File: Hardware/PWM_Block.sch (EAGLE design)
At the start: 51 parts, among them U1 PCA9685, U2 PCA9306, U3 EDISON_CONNECTOR_FULLMOUNTING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, U4 EDISON_CONNECTOR_FULLHEADER

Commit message: Added DCIN pin Corrected Header footprint Renamed board and files Cleaned up dimensions and added units Added VSYS -> VIN circuit Added DNP to pullup resistors
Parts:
- added D1: B340A, SparkFun-DiscreteSemi:DIODE-SCHOTTKY-B340A
- added SJ7: VIN_ENABLE, SparkFun-Passives:JUMPER-PAD-2-NOYES_SILK
- R4, R5: value 2.2k -> DNP
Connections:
- new net DCIN: U3.DCIN, U4.DCIN
- new net N$2: D1.C, SJ7.1
- net VCC: now also SJ7.2
- net VSYS: now also D1.A
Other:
- note added: "v02"
- note removed: "01"
- moved on the sheet: C1, C2, C3, R1, R2, R3, R4, R5, U2

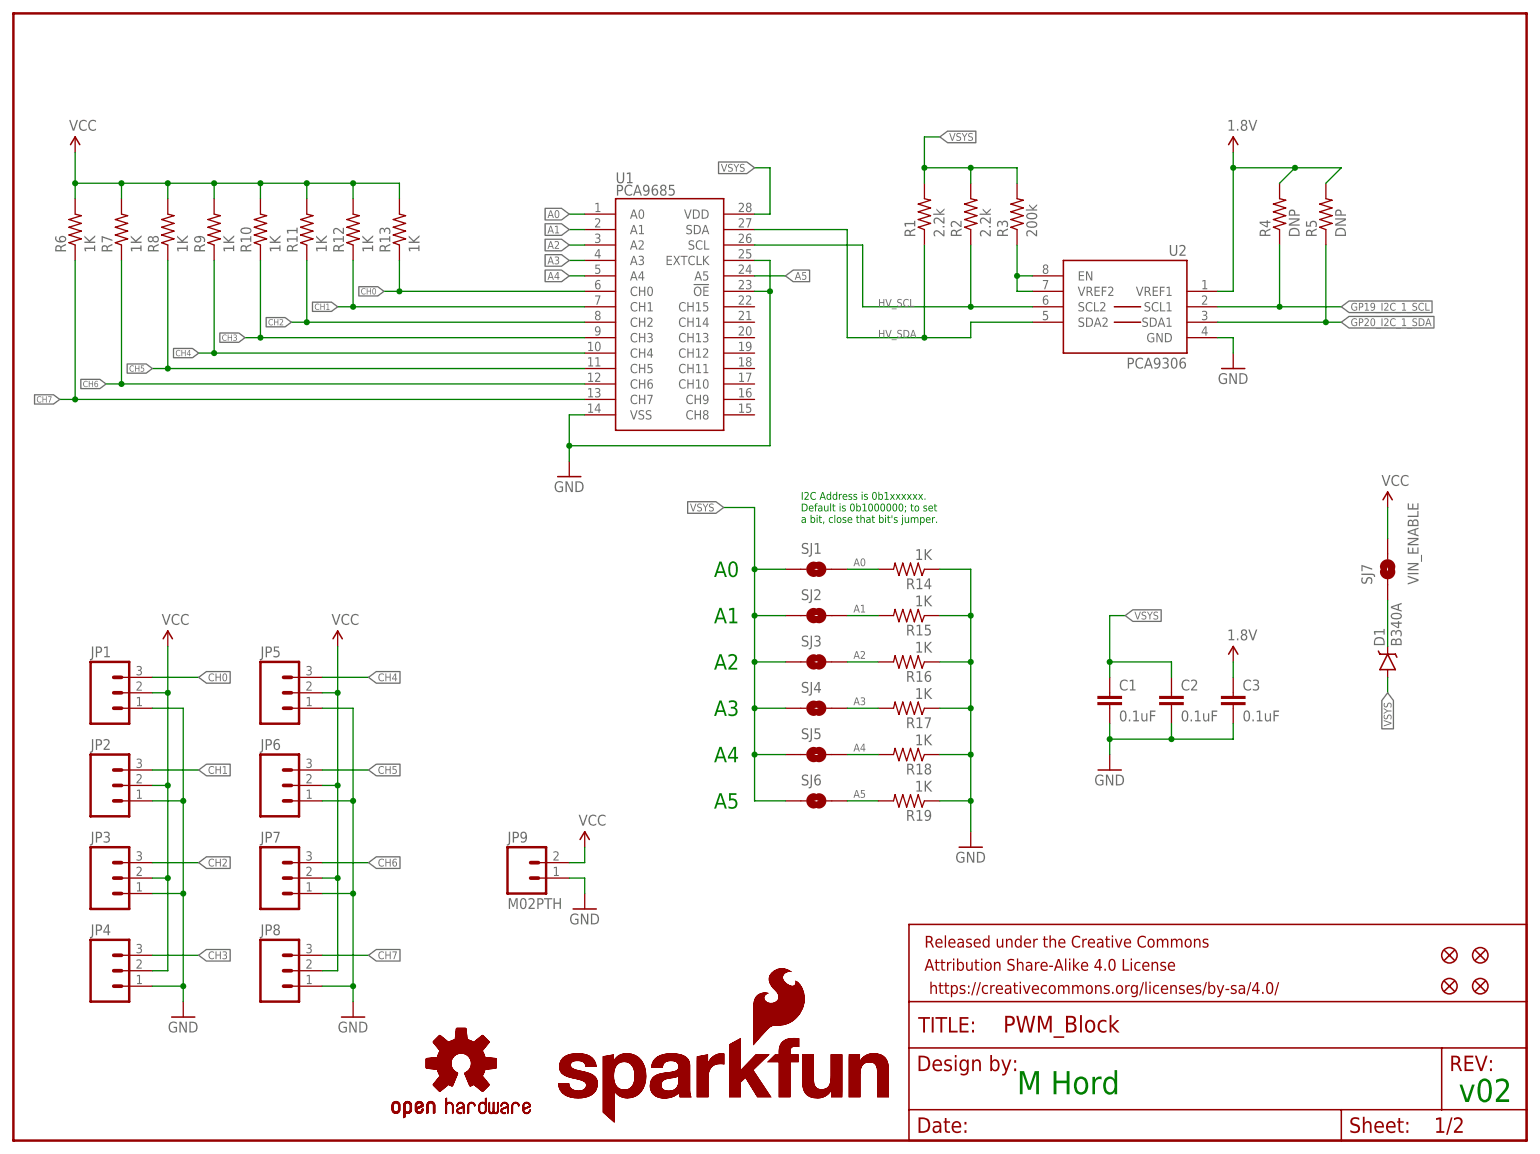
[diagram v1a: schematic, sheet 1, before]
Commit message: Rev to 10. Fix gnd and pwr, text
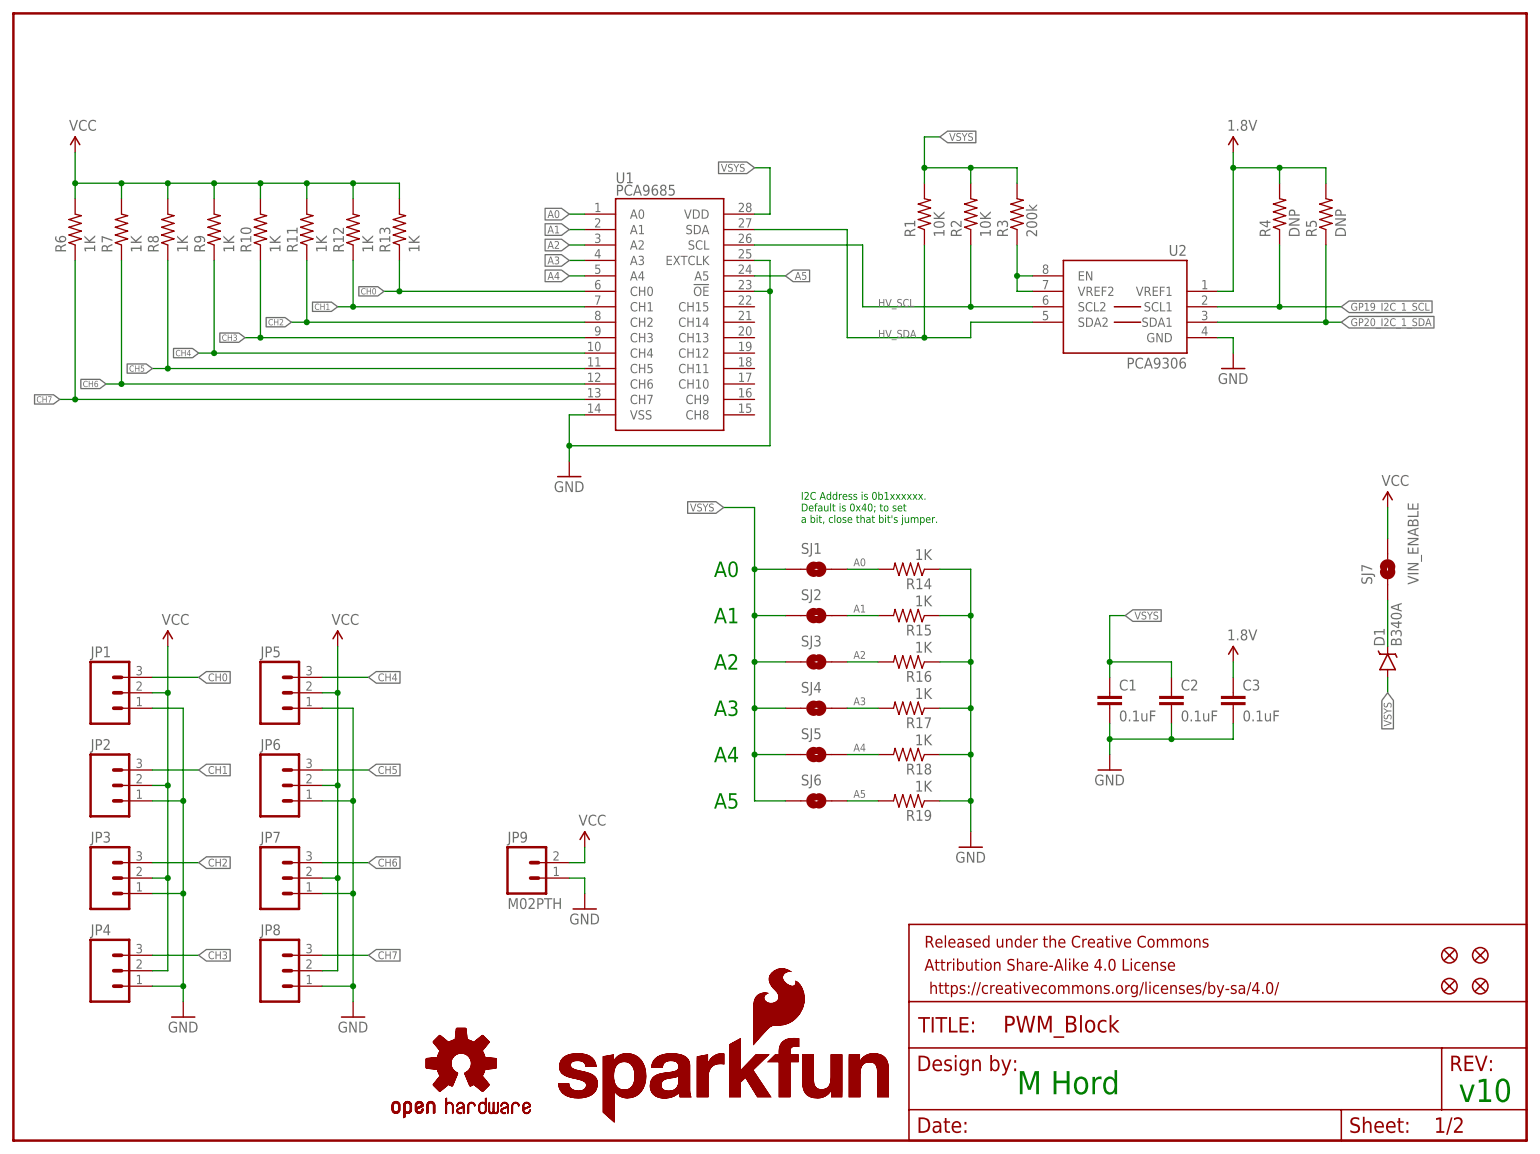
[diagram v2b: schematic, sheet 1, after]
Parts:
- R1, R2: value 2.2k -> 10K; device SparkFun-Resistors:2.2KOHM1/10W1%(0603) -> SparkFun-Resistors:10KOHM1/10W1%(0603)0603
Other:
- note added: "I2C Address is 0b1xxxxxx. Default is 0x40; to set a bit, close that bit's jumper."
- note added: "v10"
- note removed: "I2C Address is 0b1xxxxxx. Default is 0b1000000; to set a bit, close that bit's jumper."
- note removed: "v02"
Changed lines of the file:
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@@
 <?xml version="1.0" encoding="utf-8"?>
 <!DOCTYPE eagle SYSTEM "eagle.dtd">
-<eagle version="6.5.0">
+<eagle version="6.6.0">
 <drawing>
 <settings>
@@
 <layer number="254" name="cooling" color="7" fill="1" visible="yes" active="yes"/>
 </layers>
-<schematic xreflabel="%F%N/%S" xrefpart="1_/%S.%C%R">
+<schematic xreflabel="%F%N/%S" xrefpart="/%S.%C%R">
 <attributes>
 </attributes>
@@
 <part name="FRAME2" library="SparkFun-Aesthetics" deviceset="FRAME-LETTER" device=""/>
 <part name="C1" library="SparkFun-Capacitors" deviceset="0.1UF-25V(+80/-20%)(0603)" device="" value="0.1uF"/>
-<part name="R1" library="SparkFun-Resistors" deviceset="2.2KOHM1/10W1%(0603)" device="" value="2.2k"/>
-<part name="R2" library="SparkFun-Resistors" deviceset="2.2KOHM1/10W1%(0603)" device="" value="2.2k"/>
+<part name="R1" library="SparkFun-Resistors" deviceset="10KOHM1/10W1%(0603)" device="0603" value="10K"/>
+<part name="R2" library="SparkFun-Resistors" deviceset="10KOHM1/10W1%(0603)" device="0603" value="10K"/>
 <part name="U2" library="SparkFun-DigitalIC" deviceset="PCA9306" device="PCA9306DC-1:1" value="PCA9306"/>
 <part name="SUPPLY1" library="SparkFun-Aesthetics" deviceset="1.8V" device=""/>
@@
 <plain>
 <text x="165.1" y="7.62" size="3.81" layer="91">M Hord</text>
-<text x="237.744" y="6.35" size="3.81" layer="91">v02</text>
+<text x="237.744" y="6.35" size="3.81" layer="91">v10</text>
 <text x="129.54" y="101.6" size="1.27" layer="91">I2C Address is 0b1xxxxxx.
-Default is 0b1000000; to set
+Default is 0x40; to set
 a bit, close that bit's jumper.</text>
 <text x="119.38" y="93.98" size="2.54" layer="91" align="center-right">A0</text>
@@
 <pinref part="R4" gate="G$1" pin="2"/>
 <wire x1="200.66" y1="160.02" x2="200.66" y2="162.56" width="0.1524" layer="91"/>
-<wire x1="200.66" y1="160.02" x2="210.82" y2="160.02" width="0.1524" layer="91"/>
-<wire x1="210.82" y1="160.02" x2="208.28" y2="157.48" width="0.1524" layer="91"/>
+<wire x1="200.66" y1="160.02" x2="208.28" y2="160.02" width="0.1524" layer="91"/>
+<wire x1="208.28" y1="160.02" x2="208.28" y2="157.48" width="0.1524" layer="91"/>
 <junction x="200.66" y="160.02"/>
 <pinref part="R5" gate="G$1" pin="2"/>
-<wire x1="210.82" y1="160.02" x2="218.44" y2="160.02" width="0.1524" layer="91"/>
-<wire x1="218.44" y1="160.02" x2="215.9" y2="157.48" width="0.1524" layer="91"/>
-<junction x="210.82" y="160.02"/>
+<wire x1="208.28" y1="160.02" x2="215.9" y2="160.02" width="0.1524" layer="91"/>
+<wire x1="215.9" y1="160.02" x2="215.9" y2="157.48" width="0.1524" layer="91"/>
+<junction x="208.28" y="160.02"/>
 </segment>
 </net>

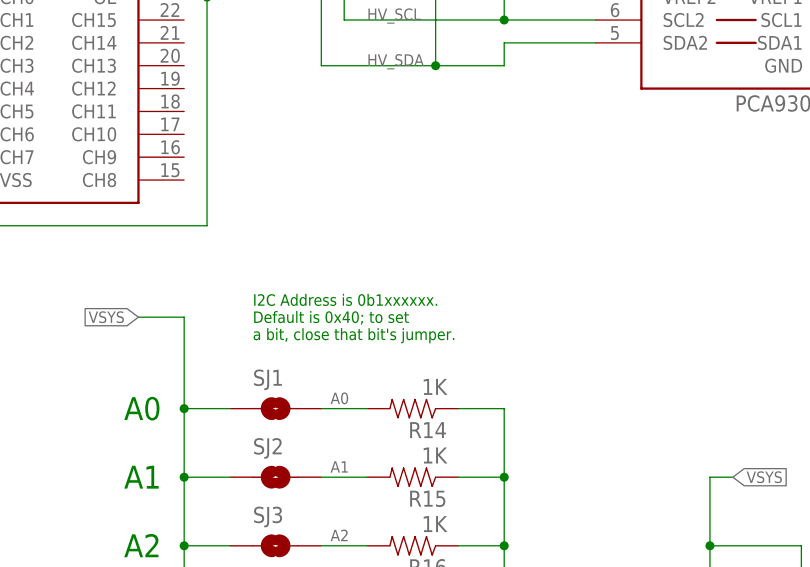
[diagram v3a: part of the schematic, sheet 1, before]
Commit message: Ready for reds Thicken VSYS->VIN trace Fix a stray ground thermal on PCA9306 No known to-do items
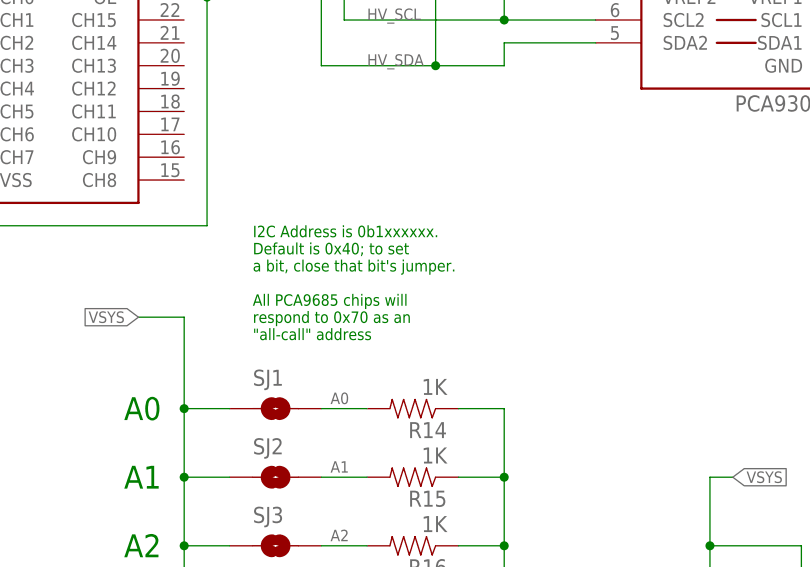
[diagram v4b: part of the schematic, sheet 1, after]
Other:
- note added: "I2C Address is 0b1xxxxxx. Default is 0x40; to set a bit, close that bit's jumper. All PCA9685 chips will respond to 0x70 as an "all-call" address"
- note removed: "I2C Address is 0b1xxxxxx. Default is 0x40; to set a bit, close that bit's jumper."
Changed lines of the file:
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@@
 <text x="129.54" y="101.6" size="1.27" layer="91">I2C Address is 0b1xxxxxx.
 Default is 0x40; to set
-a bit, close that bit's jumper.</text>
+a bit, close that bit's jumper.
+All PCA9685 chips will
+respond to 0x70 as an
+"all-call" address</text>
 <text x="119.38" y="93.98" size="2.54" layer="91" align="center-right">A0</text>
 <text x="119.38" y="86.36" size="2.54" layer="91" align="center-right">A1</text>
